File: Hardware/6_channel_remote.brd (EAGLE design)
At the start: 80 x 19.7 mm, 13 parts, among them J1 46765-0001

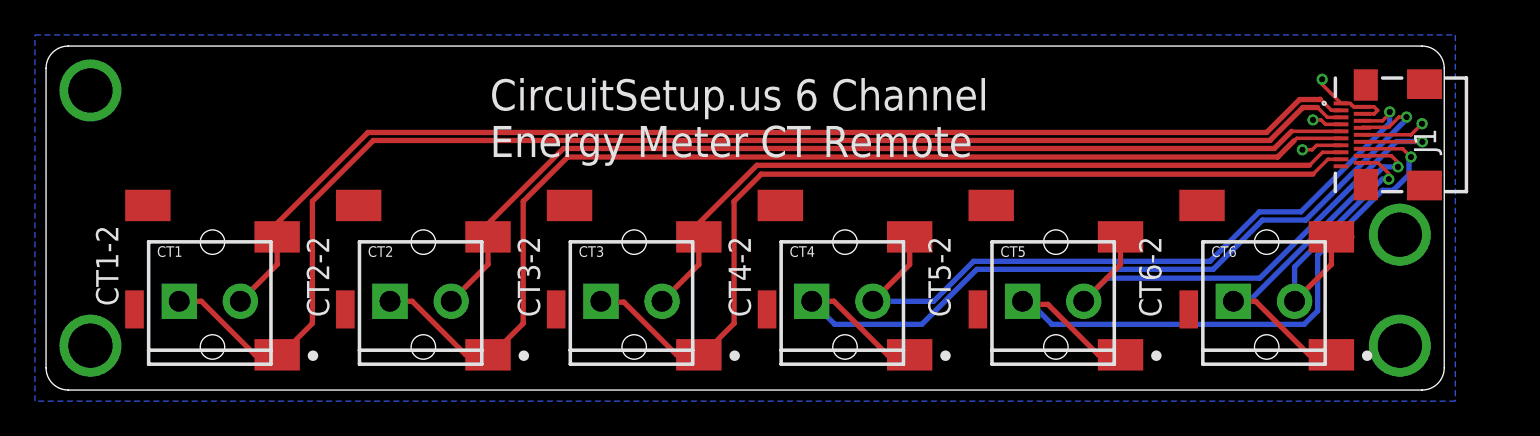
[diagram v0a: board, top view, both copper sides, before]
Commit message: v1.1 remote
- changed micro-hdmi connector to through-hole
- added mini-hdmi connector option
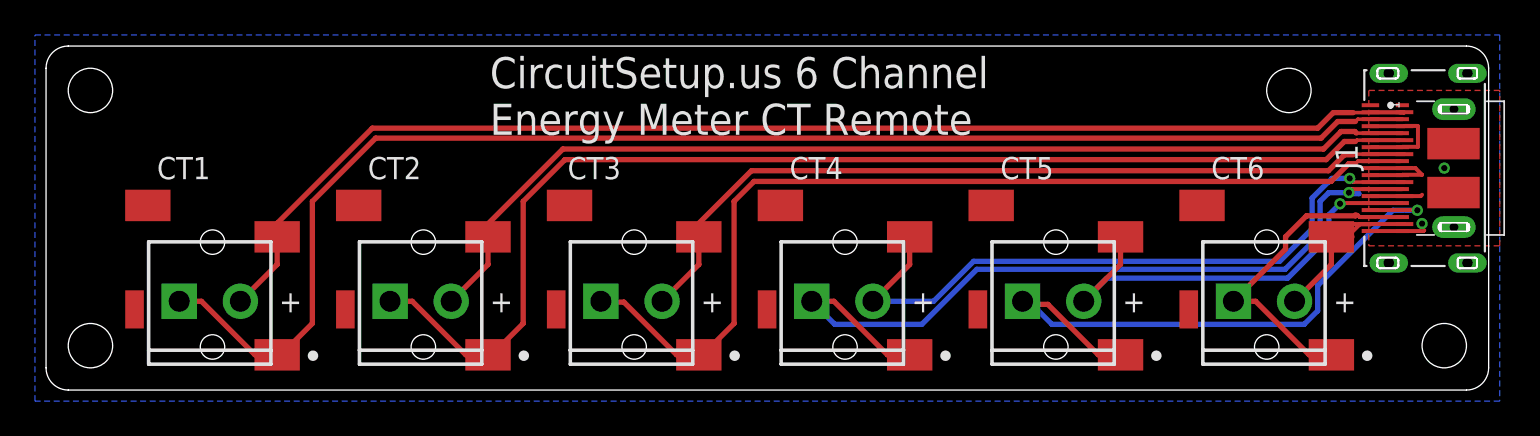
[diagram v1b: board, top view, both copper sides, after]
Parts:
- added J2: (no value), Wurth_Elektronik_Electromechanic_Input-Output_Connectors_rev19a:685119136923
- J1: value 46765-0001 -> PKS019-4011-0; device 46765-0001:46765-0001 -> SamacSys_Parts:PKS01940110
- moved J1 2.88 mm to (83.4, 12.7)
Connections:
- net GND: now also J1.11, J1.14, J1.19, J2.1, J2.10, J2.11, J2.14, J2.19, J2.4, J2.7; no longer J1.13, J1.2
- net IA+: now also J1.2, J2.2; no longer J1.3
- net IA+-2: now also J1.12, J2.12; no longer J1.6
- net IA-: now also J1.3, J2.3; no longer J1.5
- net IA--2: now also J1.13, J2.13; no longer J1.8
- net IB+: now also J1.5, J2.5; no longer J1.9
- net IB+-2: now also J1.15, J2.15; no longer J1.12
- net IB-: now also J1.6, J2.6; no longer J1.11
- net IB--2: now also J1.16, J2.16; no longer J1.14
- net IC+: now also J1.8, J2.8; no longer J1.15
- net IC+-2: now also J2.18
- net IC-: now also J1.9, J2.9; no longer J1.17
- net IC--2: now also J1.17, J2.17; no longer J1.16
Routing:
- net GND: track 12.7 -> 18.8 mm, vias 8 -> 2
- net IC-: track 52.4 -> 58.2 mm
- net IC+: track 43.8 -> 49.3 mm
- net IB+-2: track 31.2 -> 25.9 mm
- net IB-: track 64.9 -> 70.2 mm
- net IB+: track 56.3 -> 61.6 mm
- net IA+: track 69.8 -> 75.1 mm
- net IA-: track 77.9 -> 82.8 mm
- net IC+-2: track 17.3 -> 12.8 mm, vias 1 -> 0
- net IC--2: track 22.3 -> 19.1 mm, vias 1 -> 0
- net IB--2: track 39.0 -> 36.3 mm
- net IA--2: track 49.2 -> 48.6 mm
- added copper zone on layer 1, net GND
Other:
- board size 80 x 19.7 mm -> 82.5 x 19.7 mm
- board text added: "+"
- board text added: "CT1"
- board text added: "CT2"
- board text added: "CT3"
- board text added: "CT4"
- board text added: "CT5"
- board text added: "CT6"
- board text added: "Micro-HDMI cable connection Only connect to 6 Channel Energy Meter Main or Add-on Board"
